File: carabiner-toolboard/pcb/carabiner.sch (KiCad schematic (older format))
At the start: 17 parts, among them J1 CommonConnector, J7 CommonConnector

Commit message: Beta 0.1.1 of carabiner
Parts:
- Chamber1: footprint Resistor_SMD:R_0603_1608Metric_Pad1.05x0.95mm_HandSolder -> carabiner-footprints:1206_3216_HandSolder_Hole
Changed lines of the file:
@@
 F 0 "Chamber1" H 4717 3450 50  0000 C CNN
 F 1 "Thermistor" H 4717 3541 50  0000 C CNN
-F 2 "Resistor_SMD:R_0603_1608Metric_Pad1.05x0.95mm_HandSolder" H 4825 3775 50  0001 C CNN
+F 2 "carabiner-footprints:1206_3216_HandSolder_Hole" H 4825 3775 50  0001 C CNN
 F 3 "~" H 4825 3775 50  0001 C CNN
 	1    4825 3775

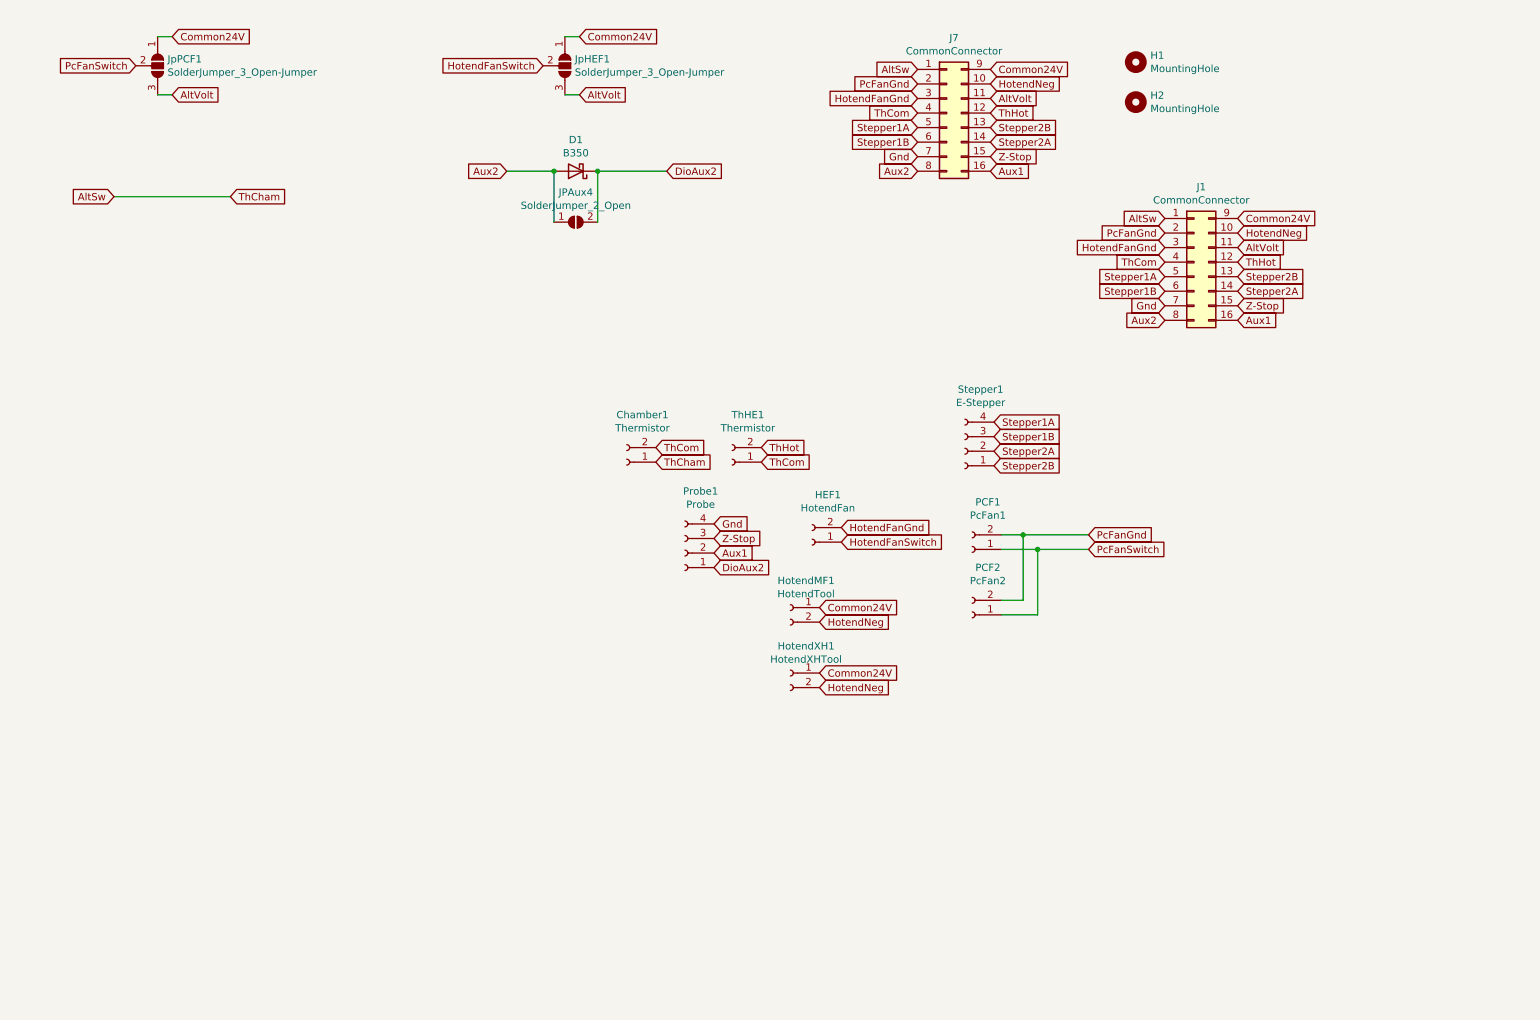
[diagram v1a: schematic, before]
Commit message: Carabiner Beta 0.2.1 Modified mounting schema (left mounting hole moved down) Modified layout of the connectors Made the horizontal MF compatible with the vertical MF (before mixing them on the 'receiver' and 'sender' would likely cause a short) Improved layout for reduced thermistor interference ChamberThermistor now supported from 0603 up to 1206
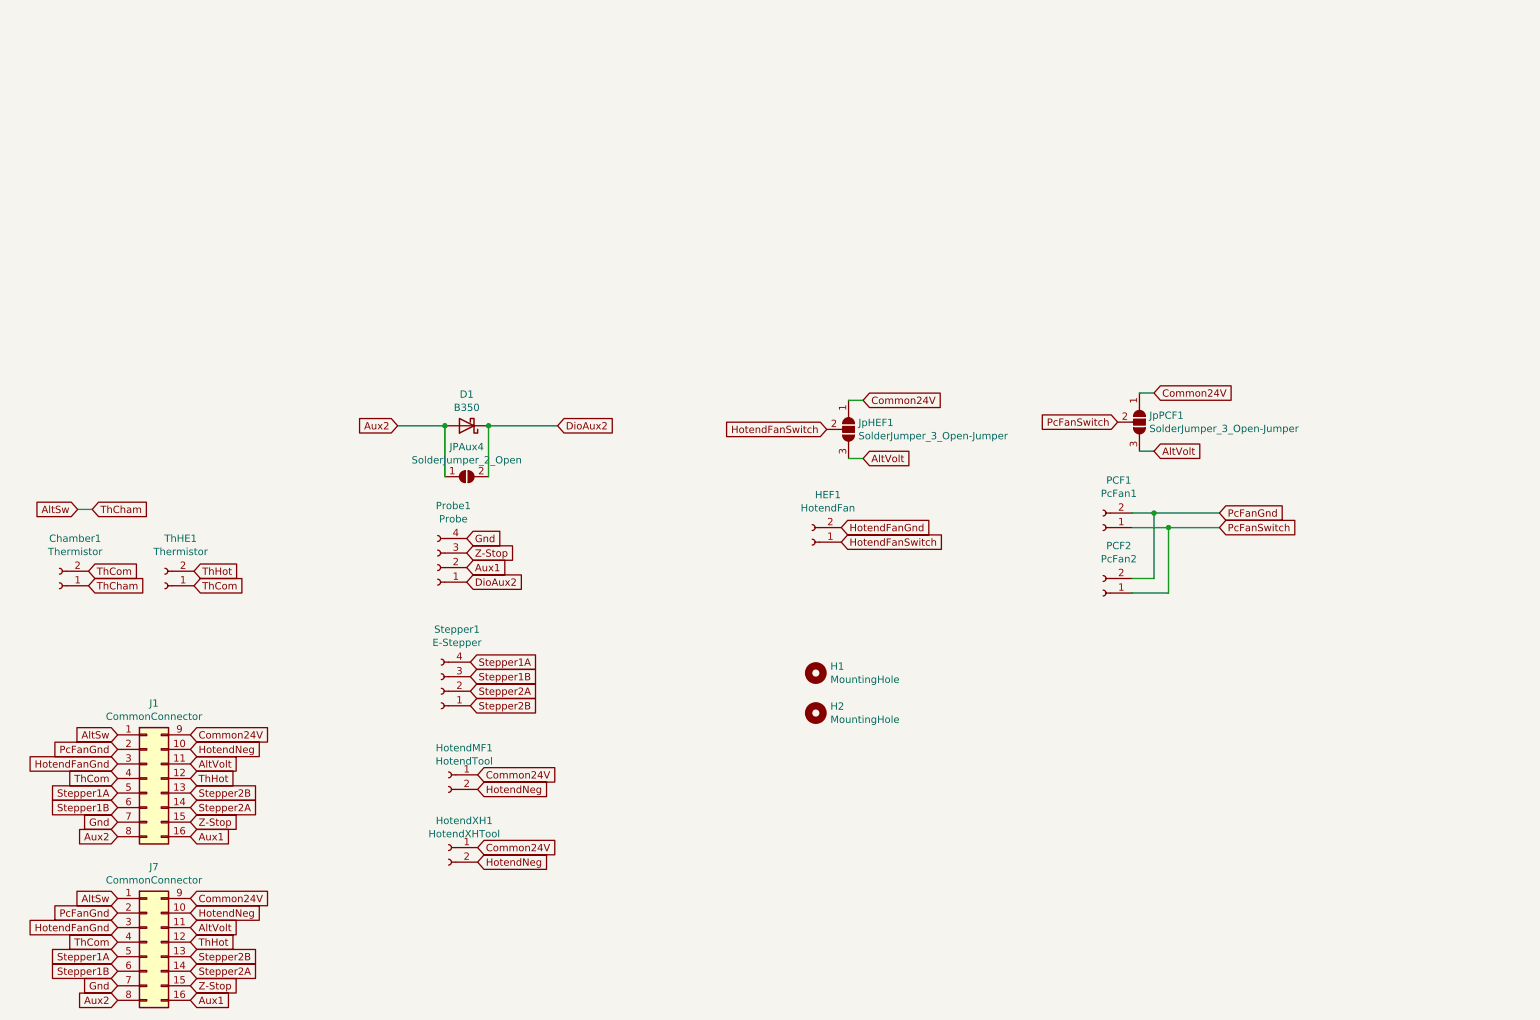
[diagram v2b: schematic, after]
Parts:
- J1: footprint carabiner-footprints:Molex_Micro-Fit_3.0_2x08_P3.00mm_Vertical -> Connector_Molex:Molex_Micro-Fit_3.0_43045-1612_2x08_P3.00mm_Vertical
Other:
- moved on the sheet: Chamber1, D1, H1, H2, HotendMF1, HotendXH1, J1, J7, JPAux4, JpHEF1, JpPCF1, PCF1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

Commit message: Carabiner Beta 0.2.2
[REFACTORING]
Rename nets to be more clear & consistent.
Refactor labels to be have more concise names
Rework traceWidth of the new nets (thinner, still more than enough power)

[FEATURE]
Split up 3-pronged jumper voltage jumper into 2 seperate ones.
Add support for new connectors:
Support 43045 1621 for the commonConnector
Support 43045 0212 for the hotendConnector
Support 43645 0215 for the thermistor
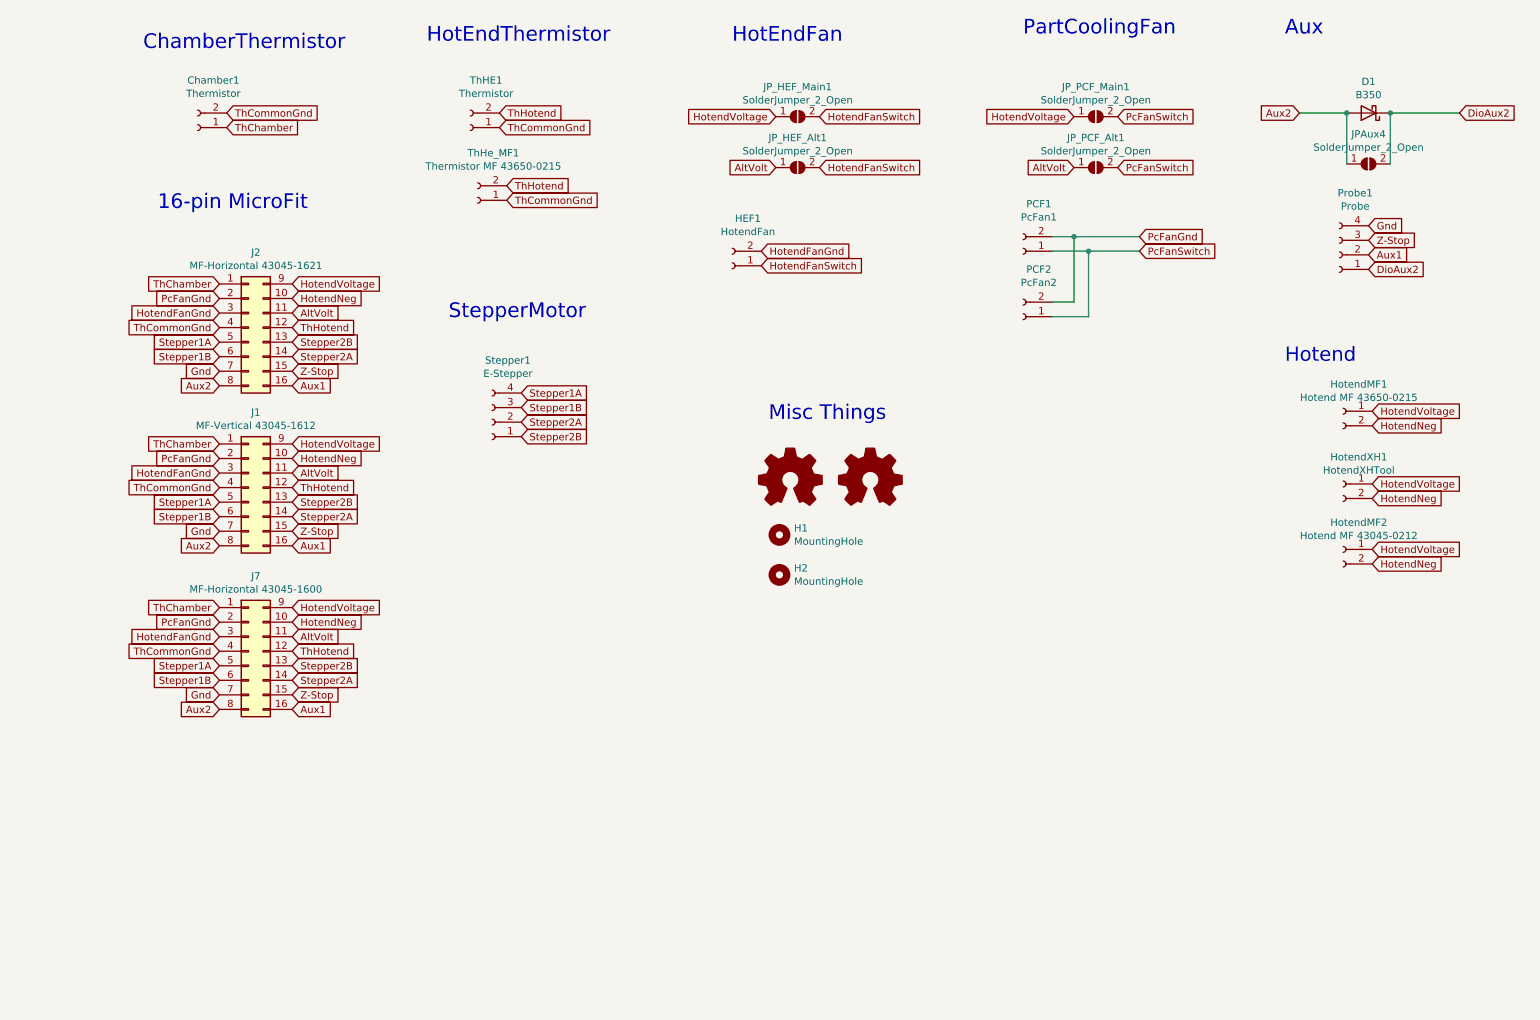
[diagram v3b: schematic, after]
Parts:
- removed JpHEF1, JpPCF1: SolderJumper_3_Open-Jumper, Jumper:SolderJumper-3_P1.3mm_Open_RoundedPad1.0x1.5mm_NumberLabels, symbol climber-rescue:SolderJumper_3_Open-Jumper
- added HotendMF2: Hotend MF 43045-0212, Connector_Molex:Molex_Micro-Fit_3.0_43045-0212_2x01_P3.00mm_Vertical, symbol climber-rescue:Conn_01x02_Female-Connector
- added J2: MF-Horizontal 43045-1621, Connector_Molex:Molex_Micro-Fit_3.0_43045-1621_2x08-1MP_P3.00mm_Horizontal, symbol climber-rescue:Conn_02x08_Top_Bottom-Connector_Generic
- added JP_HEF_Alt1, JP_HEF_Main1, JP_PCF_Alt1, JP_PCF_Main1: SolderJumper_2_Open, Jumper:SolderJumper-2_P1.3mm_Open_TrianglePad1.0x1.5mm, symbol Jumper:SolderJumper_2_Open
- added LOGO1: Logo_Open_Hardware_Small, Annex:AnnexLogo, symbol Graphic:Logo_Open_Hardware_Small
- added LOGO2: Logo_Open_Hardware_Small, Annex:AnnexLogoBack, symbol Graphic:Logo_Open_Hardware_Small
- added ThHe_MF1: Thermistor MF 43650-0215, Connector_Molex:Molex_Micro-Fit_3.0_43650-0215_1x02_P3.00mm_Vertical, symbol climber-rescue:Conn_01x02_Female-Connector
- HotendMF1: value HotendTool -> Hotend MF 43650-0215
- J1: value CommonConnector -> MF-Vertical 43045-1612
- J7: value CommonConnector -> MF-Horizontal 43045-1600
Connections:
- net AltVolt: now also J2.11 (Pin_11), JP_HEF_Alt1.1 (A), JP_PCF_Alt1.1 (A)
- net Aux1: now also J2.16 (Pin_16)
- net Aux2: now also J2.8 (Pin_8)
- net Gnd: now also J2.7 (Pin_7)
- net HotendFanGnd: now also J2.3 (Pin_3)
- net HotendFanSwitch: now also JP_HEF_Alt1.2 (B), JP_HEF_Main1.2 (B)
- net HotendNeg: now also HotendMF2.2 (Pin_2), J2.10 (Pin_10)
- net PcFanGnd: now also J2.2 (Pin_2)
- net PcFanSwitch: now also JP_PCF_Alt1.2 (B), JP_PCF_Main1.2 (B)
- net Stepper1A: now also J2.5 (Pin_5)
- net Stepper1B: now also J2.6 (Pin_6)
- net Stepper2A: now also J2.14 (Pin_14)
- net Stepper2B: now also J2.13 (Pin_13)
- net Z-Stop: now also J2.15 (Pin_15)
- net AltSw renamed ThChamber
- net ThChamber: now also J2.1 (Pin_1)
- net Common24V renamed HotendVoltage
- net HotendVoltage: now also HotendMF2.1 (Pin_1), J2.9 (Pin_9), JP_HEF_Main1.1 (A), JP_PCF_Main1.1 (A)
- net ThCom renamed ThCommonGnd
- net ThCommonGnd: now also J2.4 (Pin_4), ThHe_MF1.1 (Pin_1)
- net ThHot renamed ThHotend
- net ThHotend: now also J2.12 (Pin_12), ThHe_MF1.2 (Pin_2)
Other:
- note added: "16-pin MicroFit"
- note added: "Aux"
- note added: "ChamberThermistor"
- note added: "HotEndFan"
- note added: "HotEndThermistor"
- note added: "Hotend"
- note added: "Misc Things"
- note added: "PartCoolingFan"
- note added: "StepperMotor"
- moved on the sheet: Chamber1, D1, H1, H2, HEF1, HotendMF1, HotendXH1, J1, J7, JPAux4, PCF1, PCF2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
